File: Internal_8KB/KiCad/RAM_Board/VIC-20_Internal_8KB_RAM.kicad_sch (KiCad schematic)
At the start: 9 parts, among them J1 UD4, J2 UE4, J3 SW, J4 Signals, U1 6264, U2 GAL16V8

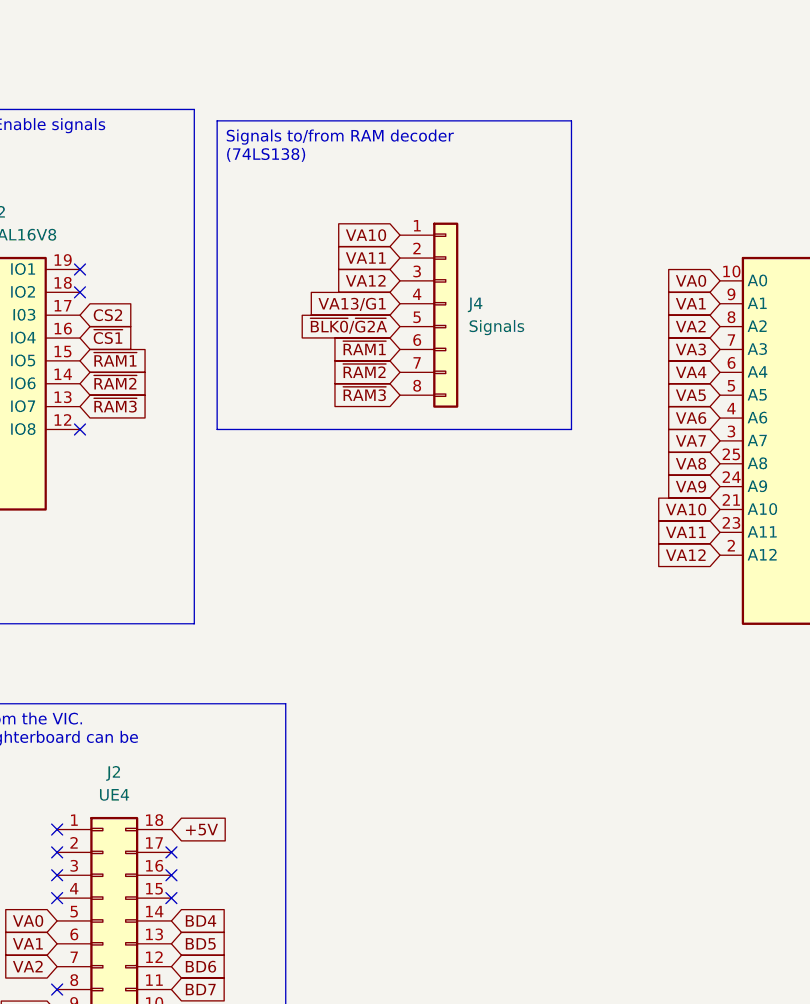
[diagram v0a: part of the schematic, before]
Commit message: Rename VIC20 to VIC-20
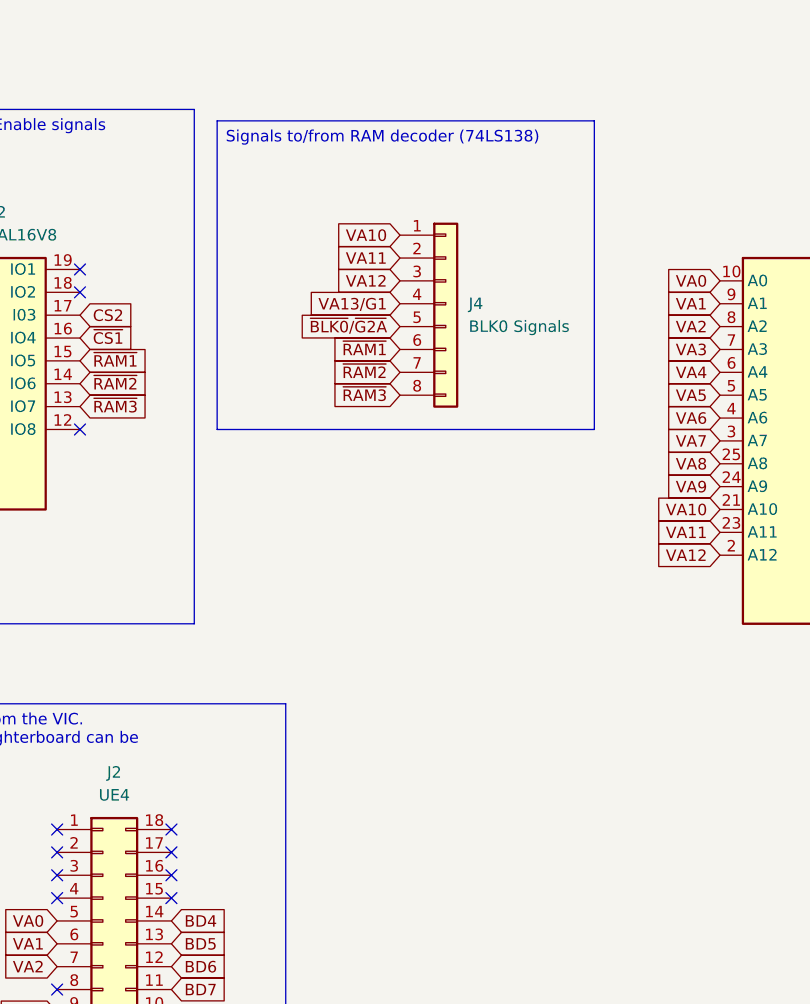
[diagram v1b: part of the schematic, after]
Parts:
- J4: value Signals -> BLK0 Signals
- U1: footprint Package_DIP:DIP-28_W15.24mm_Socket -> Package_DIP:DIP-28_W15.24mm
- U2: footprint Package_DIP:DIP-20_W7.62mm_Socket -> Package_DIP:DIP-20_W7.62mm
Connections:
- net +5V: no longer J2.18 (Pin_18)
- no-connect marks 18 -> 19
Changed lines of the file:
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@@
 		(exclude_from_sim no)
 		(at 76.2 26.67 0)
-		(size 39.37 34.29)
+		(size 41.91 34.29)
 		(margins 0.9525 0.9525 0.9525 0.9525)
 		(stroke
@@
 	)
 	(no_connect
+		(at 71.12 105.41)
+	)
+	(no_connect
 		(at 58.42 105.41)
 	)
@@
 		(property "Intersheetrefs" "${INTERSHEET_REFS}"
 			(at 164.2147 59.69 0)
-			(effects
-				(font
-					(size 1.27 1.27)
-				)
-				(justify left)
-				(hide yes)
-			)
-		)
-	)
-	(global_label "+5V"
-		(shape input)
-		(at 71.12 105.41 0)
-		(fields_autoplaced yes)
-		(effects
-			(font
-				(size 1.27 1.27)
-			)
-			(justify left)
-		)
-		(property "Intersheetrefs" "${INTERSHEET_REFS}"
-			(at 77.9757 105.41 0)
 			(effects
 				(font
@@
 			)
 		)
-		(property "Footprint" "Package_DIP:DIP-20_W7.62mm_Socket"
+		(property "Footprint" "Package_DIP:DIP-20_W7.62mm"
 			(at 48.26 55.88 0)
 			(effects
@@
 			)
 		)
-		(property "Value" "Signals"
+		(property "Value" "BLK0 Signals"
 			(at 104.14 49.5299 0)
 			(effects
@@
 			)
 		)
-		(property "Footprint" "Package_DIP:DIP-28_W15.24mm_Socket"
+		(property "Footprint" "Package_DIP:DIP-28_W15.24mm"
 			(at 144.78 64.77 0)
 			(effects
